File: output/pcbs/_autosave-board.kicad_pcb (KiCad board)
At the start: 2 copper layers, 162.1 x 157 mm, 65 parts, among them J1 Jumper, J2 Jumper

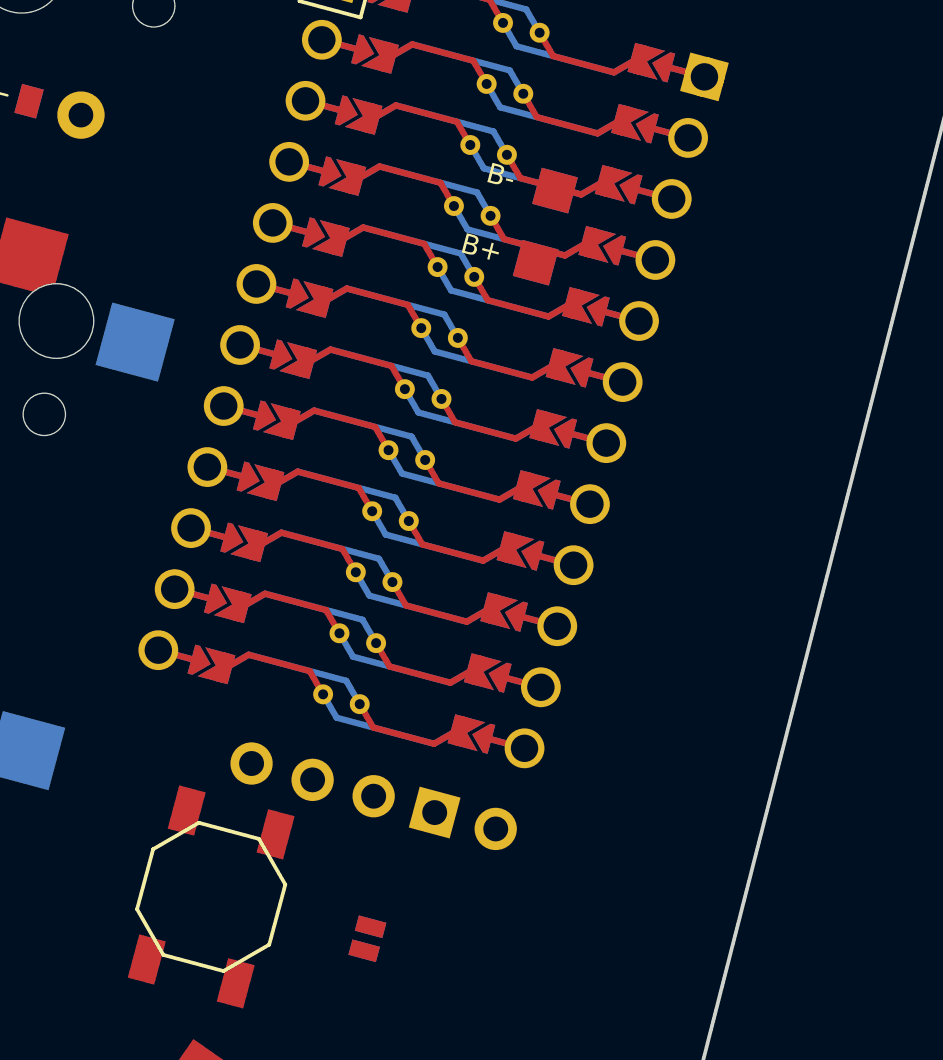
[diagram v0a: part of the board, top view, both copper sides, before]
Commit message: migrate ergogen 4
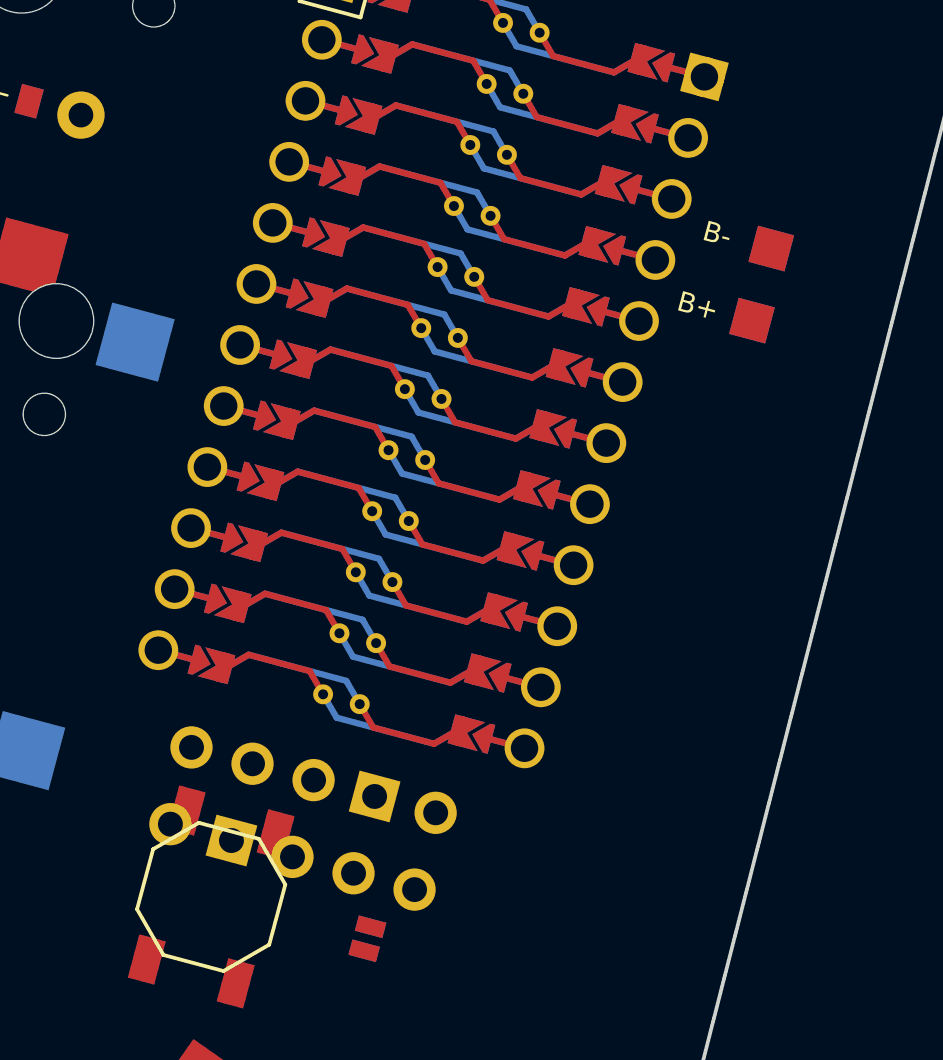
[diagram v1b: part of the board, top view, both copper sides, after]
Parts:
- added OLED2: OLED, lib:OLED_headers, F.Cu at (119.4, 25.8)
- moved PAD1 9.00 mm to (130.4, 3.89)
- moved PAD2 9.00 mm to (131.2, 0.99)
- moved OLED1 2.50 mm to (105.4, 22.0)
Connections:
- D10 pad 2: ring_home -> P6
- D12 pad 1: P4 -> ring_num
- D12 pad 2: P4 -> ring_num
- D13 pad 1: P7 -> middle_bottom
- D14 pad 2: P6 -> middle_home
- D15 pad 2: P5 -> middle_top
- D16 pad 2: P4 -> middle_num
- D17 pad 1: P7 -> index_bottom
- D18 pad 1: P6 -> index_home
- D19 pad 1: P5 -> index_top
- D2 pad 2: P6 -> outer_home
- D20 pad 2: index_num -> P4
- D23 pad 1: inner_top -> P5
- D24 pad 2: inner_num -> P4
- D25 pad 1: P3 -> near1_home
- D25 pad 2: near1_home -> P3
- D27 pad 2: home_home -> P3
- D28 pad 2: P3 -> home_top
- D4 pad 1: P4 -> outer_num
- D5 pad 1: pinky_bottom -> P7
- D5 pad 2: pinky_bottom -> P7
- D6 pad 1: pinky_home -> P6
- D7 pad 1: P5 -> pinky_top
- D7 pad 2: pinky_top -> P5
- D8 pad 1: pinky_num -> P4
